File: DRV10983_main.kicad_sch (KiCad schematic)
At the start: 10 parts, among them J1 Conn_01x03_Socket, U1 DRV10983QPWPRQ1

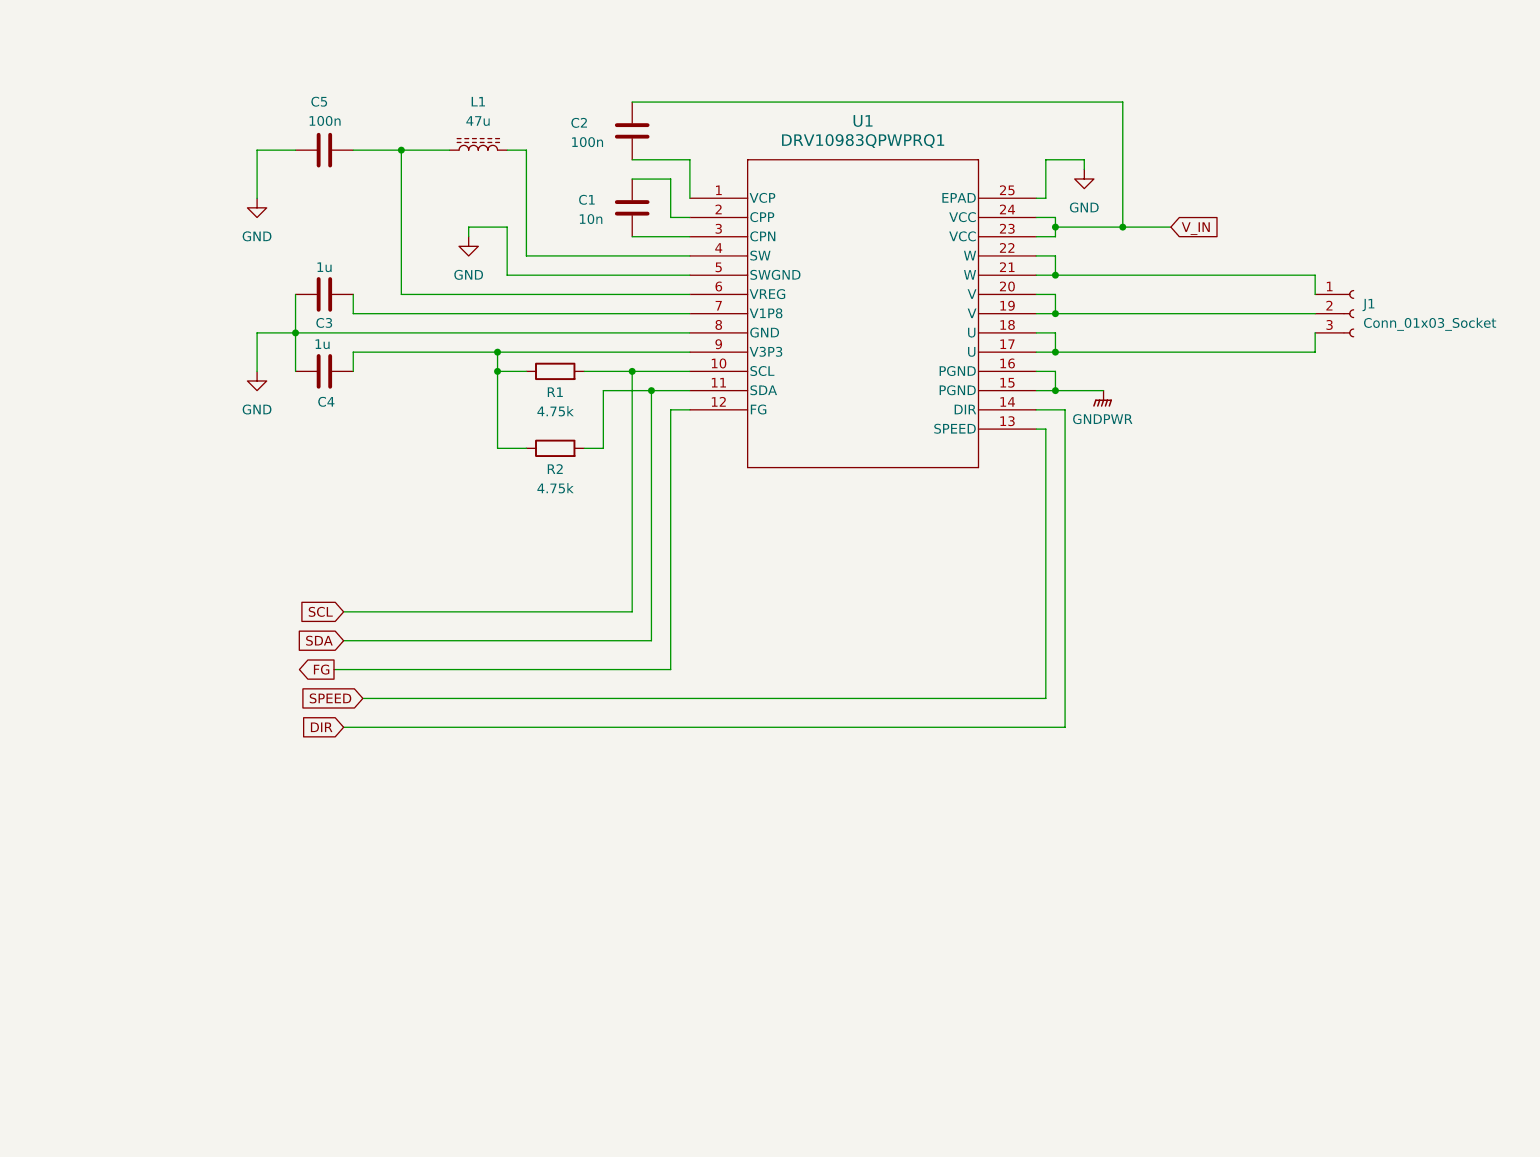
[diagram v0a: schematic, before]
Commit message: Schematic complete
Completed power and controller sub-schematics, ESD protection

Not completed: componenet values and footprints

Not started: PCB layout design
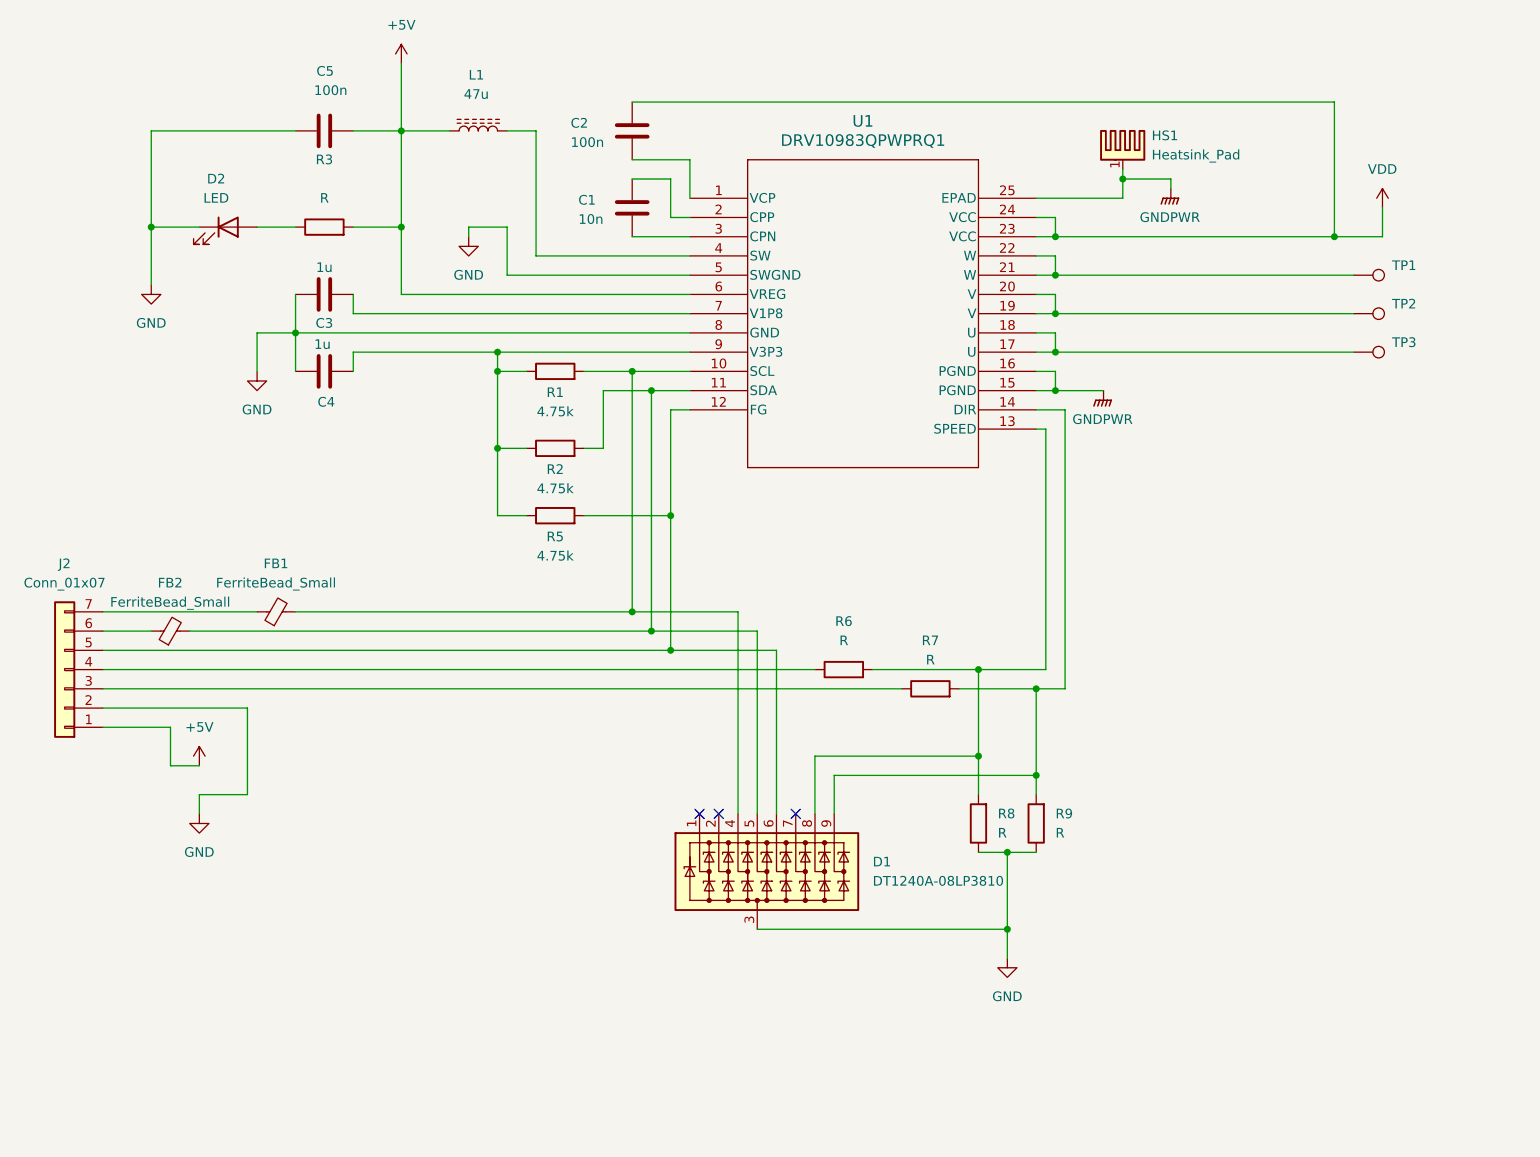
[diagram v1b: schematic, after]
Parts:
- removed J1: Conn_01x03_Socket, symbol Connector:Conn_01x03_Socket
- added D1: DT1240A-08LP3810, Package_DFN_QFN:UDFN-9_1.0x3.8mm_P0.5mm, symbol Power_Protection:DT1240A-08LP3810
- added D2: LED, symbol Device:LED
- added FB1, FB2: FerriteBead_Small, symbol Device:FerriteBead_Small
- added HS1: Heatsink_Pad, symbol Mechanical:Heatsink_Pad
- added J2: Conn_01x07, Connector_JST:JST_PH_S7B-PH-K_1x07_P2.00mm_Horizontal, symbol Connector_Generic:Conn_01x07
- added R3, R6, R7, R8, R9: R, symbol Device:R
- added R5: 4.75k, Resistor_SMD:R_0603_1608Metric, symbol Device:R
- added TP1, TP2, TP3: TestPoint, TestPoint:TestPoint_Pad_4.0x4.0mm, symbol Connector:TestPoint
- R2: footprint (none) -> Resistor_SMD:R_0603_1608Metric
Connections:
- net GND: now also D1.3 (A), D2.1 (K), J2.2 (Pin_2), R8.1, R9.1; no longer U1.25 (EPAD)
- net GNDPWR: now also U1.25 (EPAD), HS1.1
- net at C4.2, R1.1, R2.1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: now also R5.1
- net +5V: now reaches C5.2, L1.1, U1.6 (VREG)
- net +5V: now also J2.1 (Pin_1), R3.2
- net at U1.17 (U), U1.18 (U): now also TP3.1
- net at U1.19 (V), U1.20 (V): now also TP2.1
- net at U1.21 (W), U1.22 (W): now also TP1.1
- net DIR: no longer names the net of U1.14 (DIR)
- net DIR: now also D1.9 (K8), R7.2, R9.2
- net FG: no longer names the net of U1.12 (FG)
- net FG: now also D1.6 (K5), J2.5 (Pin_5), R5.2
- net SCL: no longer names the net of R1.2, U1.10 (SCL)
- net SCL: now also D1.4 (K3), FB1.2
- net SDA: no longer names the net of R2.2, U1.11 (SDA)
- net SDA: now also D1.5 (K4), FB2.2
- net SPEED: no longer names the net of U1.13 (SPEED)
- net SPEED: now also D1.8 (K7), R6.2, R8.2
- net V_IN renamed VDD
- new net: J2.4 (Pin_4), R6.1
- new net: FB2.1, J2.6 (Pin_6)
- new net: J2.3 (Pin_3), R7.1
- new net: D2.2 (A), R3.1
- new net: FB1.1, J2.7 (Pin_7)
- no-connect marks 0 -> 3
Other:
- title: (none) -> Motor controller
- moved on the sheet: C5, L1

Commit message: PCB v1 complete
with images, README extended...
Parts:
- removed D1: DT1240A-08LP3810, Package_DFN_QFN:UDFN-9_1.0x3.8mm_P0.5mm, symbol Power_Protection:DT1240A-08LP3810
- added H1, H2, H3, H4: MountingHole, MountingHole:MountingHole_2.7mm_Pad, symbol Mechanical:MountingHole
- C1, C2, C3, C4, C5: footprint (none) -> Capacitor_SMD:C_0603_1608Metric
- D2: footprint (none) -> LED_SMD:LED_0603_1608Metric
- FB1, FB2: value FerriteBead_Small -> 0.8 - 2k2; footprint (none) -> Inductor_SMD:L_0603_1608Metric
- HS1: footprint (none) -> TestPoint:TestPoint_Pad_4.0x4.0mm
- L1: footprint (none) -> VLS6045EX-470M:IND_VLS6045EX-470M
- R1: footprint (none) -> Resistor_SMD:R_0603_1608Metric
- R3: value R -> 150; footprint (none) -> Resistor_SMD:R_0603_1608Metric
- R6, R7: value R -> 4k7; footprint (none) -> Resistor_SMD:R_0603_1608Metric
- R8, R9: value R -> 9k1; footprint (none) -> Resistor_SMD:R_0603_1608Metric
- TP1, TP2, TP3: footprint TestPoint:TestPoint_Pad_4.0x4.0mm -> TestPoint:TestPoint_Pad_3.0x3.0mm
- U1: footprint PWP24_2P4X5P16_TEX -> DRV 10893 - Q1:PWP24_2P4X5P16_TEX
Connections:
- net MOT_V: now reaches TP2.1, U1.19 (V), U1.20 (V)
- net at FB2.1: now also J2.7 (Pin_7); no longer J2.6 (Pin_6)
- net MOT_U: now reaches TP3.1, U1.17 (U), U1.18 (U)
- net MOT_W: now reaches TP1.1, U1.21 (W), U1.22 (W)
- net at FB1.1: now also J2.6 (Pin_6); no longer J2.7 (Pin_7)
- no-connect marks 3 -> 0
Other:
- moved on the sheet: R6
